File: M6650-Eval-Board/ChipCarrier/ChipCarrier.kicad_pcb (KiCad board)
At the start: 2 copper layers, 39.4 x 33 mm, 10 parts, among them J1 BB, J2 BR, J3 BT, J4 BL, U1 MSM6650GS-BK, Y1 4.096M

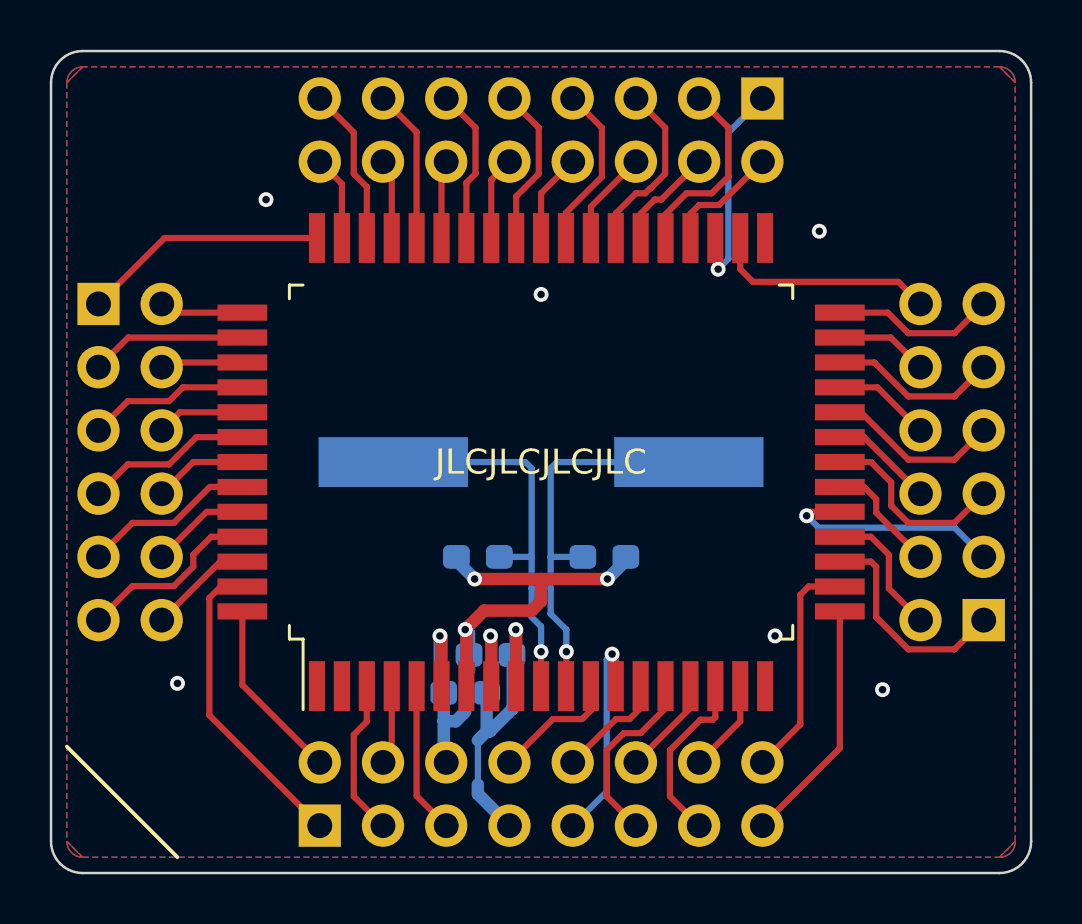
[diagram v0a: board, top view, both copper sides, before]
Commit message: Add debounce to manual parallel board, redo board edges and clearance rules
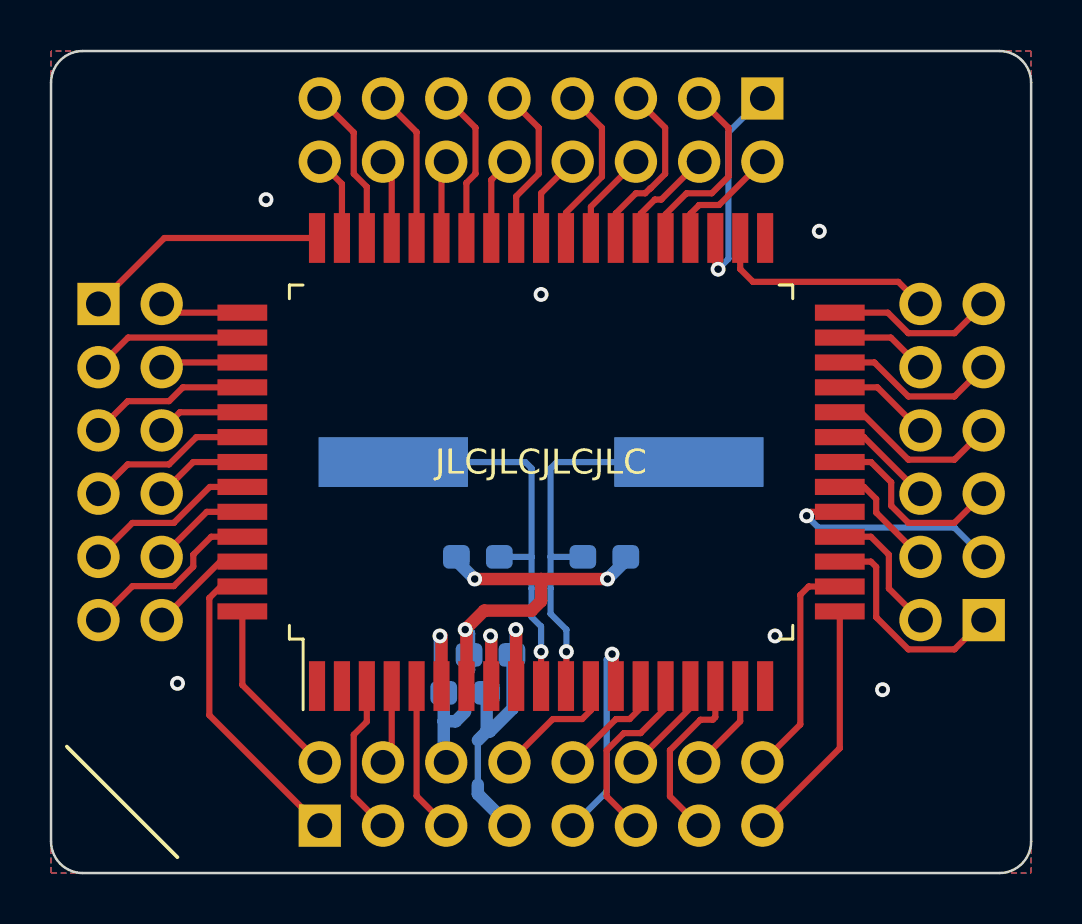
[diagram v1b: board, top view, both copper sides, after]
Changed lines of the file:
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@@
   (segment (start 20.13 33.845) (end 17.78 36.195) (width 0.25) (layer "F.Cu") (net 62))
   (zone (net 2) (net_name "/GND") (layers "F&B.Cu") (hatch edge 0.5)
-    (connect_pads (clearance 0))
+    (connect_pads (clearance 0.25))
     (min_thickness 0.25) (filled_areas_thickness no)
-    (fill yes (thermal_gap 0.5) (thermal_bridge_width 0.5))
+    (fill yes (thermal_gap 0.4) (thermal_bridge_width 0.5))
     (polygon
       (pts
-        (xy 52.07 45.085)
-        (xy 51.435 45.72)
-        (xy 51.506358 45.718318)
-        (xy 51.645495 45.686561)
-        (xy 51.774078 45.624639)
-        (xy 51.885657 45.535657)
-        (xy 51.974639 45.424078)
-        (xy 52.036561 45.295495)
-        (xy 52.068318 45.156358)
+        (xy 52.705 13.335)
+        (xy 13.335 13.335)
+        (xy 13.335 46.355)
+        (xy 52.705 46.355)
       )
     )
-  )
-  (zone (net 2) (net_name "/GND") (layers "F&B.Cu") (hatch edge 0.5)
-    (connect_pads (clearance 0))
-    (min_thickness 0.25) (filled_areas_thickness no)
-    (fill yes (thermal_gap 0.5) (thermal_bridge_width 0.5))
-    (polygon
-      (pts
-        (xy 13.97 14.605)
-        (xy 14.605 13.97)
-        (xy 14.533642 13.971682)
-        (xy 14.394505 14.003439)
-        (xy 14.265922 14.065361)
-        (xy 14.154343 14.154343)
-        (xy 14.065361 14.265922)
-        (xy 14.003439 14.394505)
-        (xy 13.971682 14.533642)
-      )
-    )
-  )
-  (zone (net 2) (net_name "/GND") (layers "F&B.Cu") (hatch edge 0.5)
-    (connect_pads (clearance 0.5))
-    (min_thickness 0.25) (filled_areas_thickness no)
-    (fill yes (thermal_gap 0.5) (thermal_bridge_width 0.5))
-    (polygon
-      (pts
-        (xy 51.435182 13.97)
-        (xy 14.605 13.97)
-        (xy 13.97 14.604746)
-        (xy 13.97 45.085)
-        (xy 14.605 45.72)
-        (xy 51.435 45.72)
-        (xy 52.07 45.085)
-        (xy 52.07 14.605)
-      )
-    )
-  )
-  (zone (net 2) (net_name "/GND") (layers "F&B.Cu") (hatch edge 0.5)
-    (connect_pads (clearance 0))
-    (min_thickness 0.25) (filled_areas_thickness no)
-    (fill yes (thermal_gap 0.5) (thermal_bridge_width 0.5))
-    (polygon
-      (pts
-        (xy 51.435 13.97)
-        (xy 52.07 14.605)
-        (xy 52.068318 14.533642)
-        (xy 52.036561 14.394505)
-        (xy 51.974639 14.265922)
-        (xy 51.885657 14.154343)
-        (xy 51.774078 14.065361)
-        (xy 51.645495 14.003439)
-        (xy 51.506358 13.971682)
-      )
-    )
-  )
-  (zone (net 2) (net_name "/GND") (layers "F&B.Cu") (hatch edge 0.5)
-    (connect_pads (clearance 0))
-    (min_thickness 0.25) (filled_areas_thickness no)
-    (fill yes (thermal_gap 0.5) (thermal_bridge_width 0.5))
-    (polygon
-      (pts
-        (xy 14.605 45.72)
-        (xy 13.97 45.085)
-        (xy 13.971682 45.156358)
-        (xy 14.003439 45.295495)
-        (xy 14.065361 45.424078)
-        (xy 14.154343 45.535657)
-        (xy 14.265922 45.624639)
-        (xy 14.394505 45.686561)
-        (xy 14.533642 45.718318)
-      )
-    )
